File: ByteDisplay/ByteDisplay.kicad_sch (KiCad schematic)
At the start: 22 parts, among them J1 Conn_01x08_Pin, J2 Conn_01x01_Socket, J3 Conn_01x01_Socket, J4 Conn_01x01_Socket, U1 74HCT573

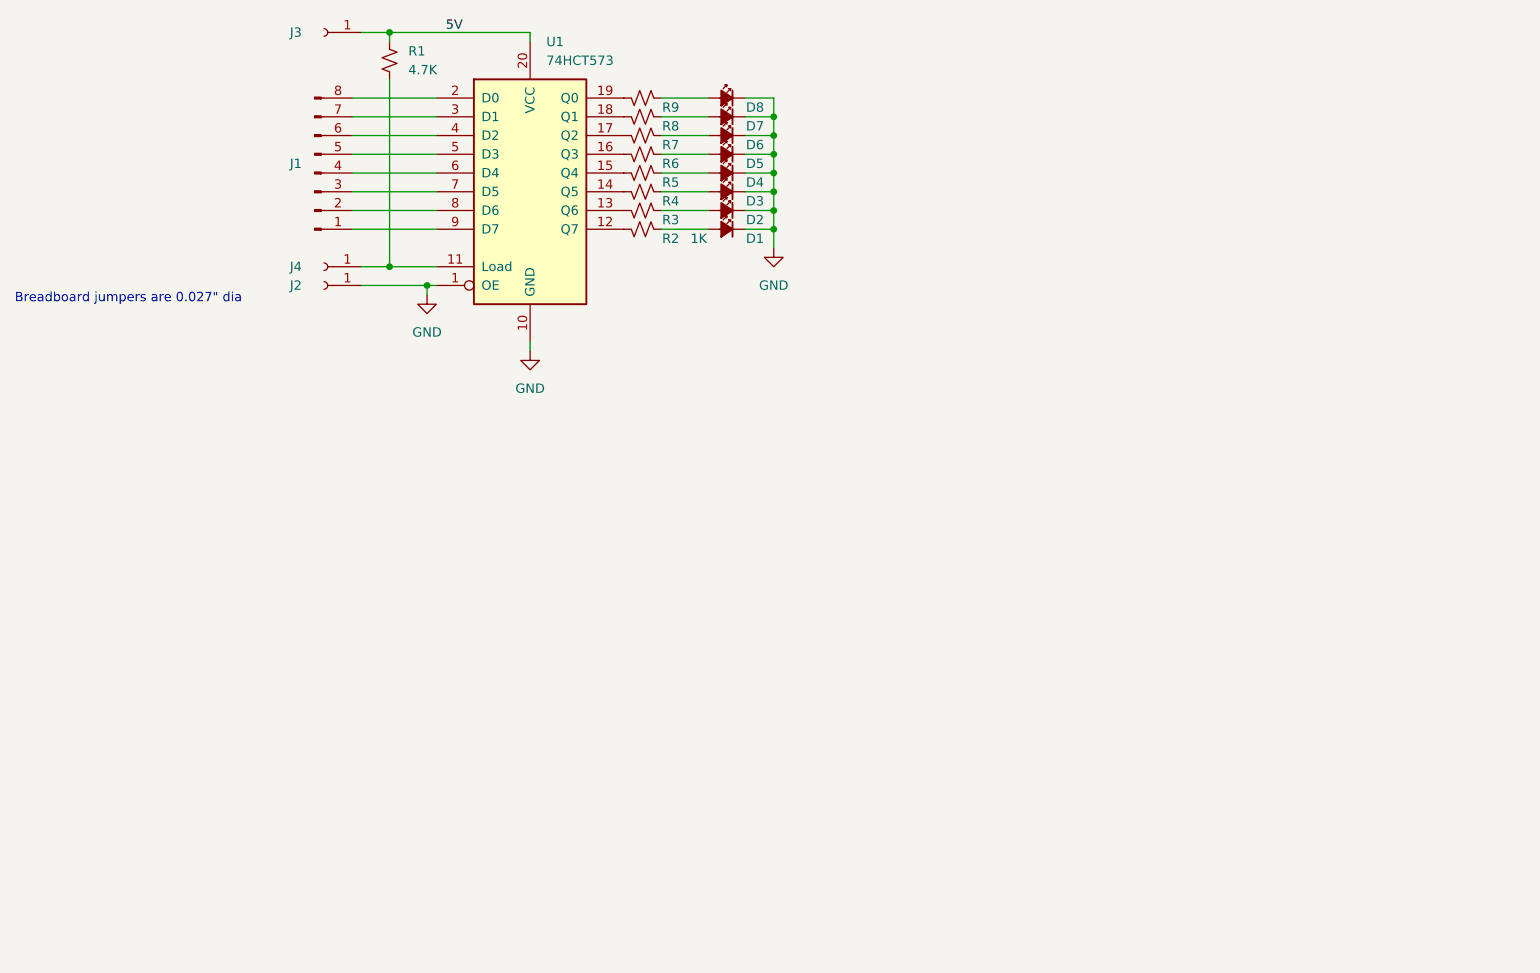
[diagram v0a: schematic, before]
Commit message: Add pullup resistors to ClockGen and ByteHex
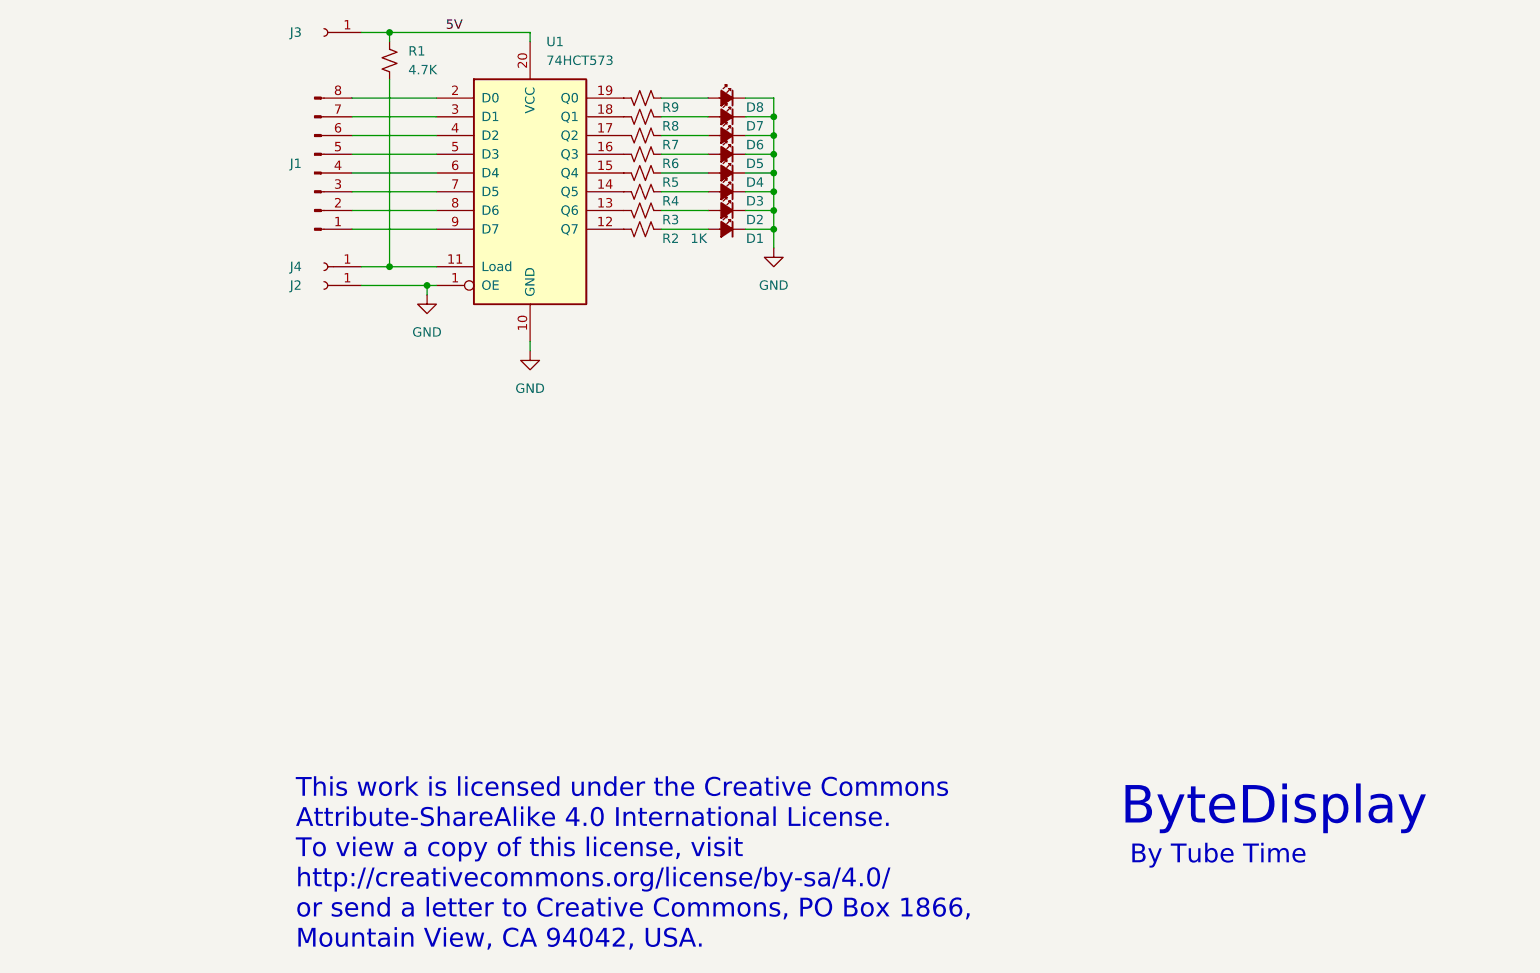
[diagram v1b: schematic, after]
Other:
- note added: "By Tube Time"
- note added: "ByteDisplay"
- note added: "This work is licensed under the Creative Commons Attribute-ShareAlike 4.0 International License. To view a copy of this license, visit http://creativecommons.org/license/by-sa/4.0/ or send a letter to Creative Commons, PO Box 1866, Mountain View, CA 94042, USA."
- note removed: "Breadboard jumpers are 0.027" dia"
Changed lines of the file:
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@@
     (stroke (width 0) (type default))
   )
-  (text "Breadboard jumpers are 0.027\" dia\n" (at 29.21 102.87 0)
-    (effects (font (size 1.27 1.27)) (justify left bottom))
+  (text "This work is licensed under the Creative Commons\nAttribute-ShareAlike 4.0 International License.\nTo view a copy of this license, visit\nhttp://creativecommons.org/license/by-sa/4.0/\nor send a letter to Creative Commons, PO Box 1866,\nMountain View, CA 94042, USA."
+    (at 67.31 190.5 0)
+    (effects (font (size 2.54 2.54)) (justify left bottom))
+  )
+  (text "ByteDisplay" (at 179.07 173.99 0)
+    (effects (font (size 5.08 5.08)) (justify left bottom))
+  )
+  (text "By Tube Time" (at 180.34 179.07 0)
+    (effects (font (size 2.54 2.54)) (justify left bottom))
   )
   (label "5V" (at 87.63 66.04 0) (fields_autoplaced)
